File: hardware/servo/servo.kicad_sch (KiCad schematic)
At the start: 87 parts, among them J1 Midi In, J2 Midi Thru, J3 NeoPixel, J4 Power, J6 I2C0, J7 I2C1, M1 Motor_Servo, M10 Motor_Servo, M11 Motor_Servo, M12 Motor_Servo, M13 Motor_Servo, M14 Motor_Servo, M15 Motor_Servo, M16 Motor_Servo, M2 Motor_Servo, M3 Motor_Servo, M4 Motor_Servo, M5 Motor_Servo, M6 Motor_Servo, M7 Motor_Servo, M8 Motor_Servo, M9 Motor_Servo, Q1 BSS138, Q2 BSS138, Q3 TSM680P06, SW1 Reset, U1 6N138, U2 74AHC1G125, U3 74AHC1G125, U4 Raspberry Pi Pico, U5 AZ1117-5.0, U6 AZ1117-5.0, U7 GS8331

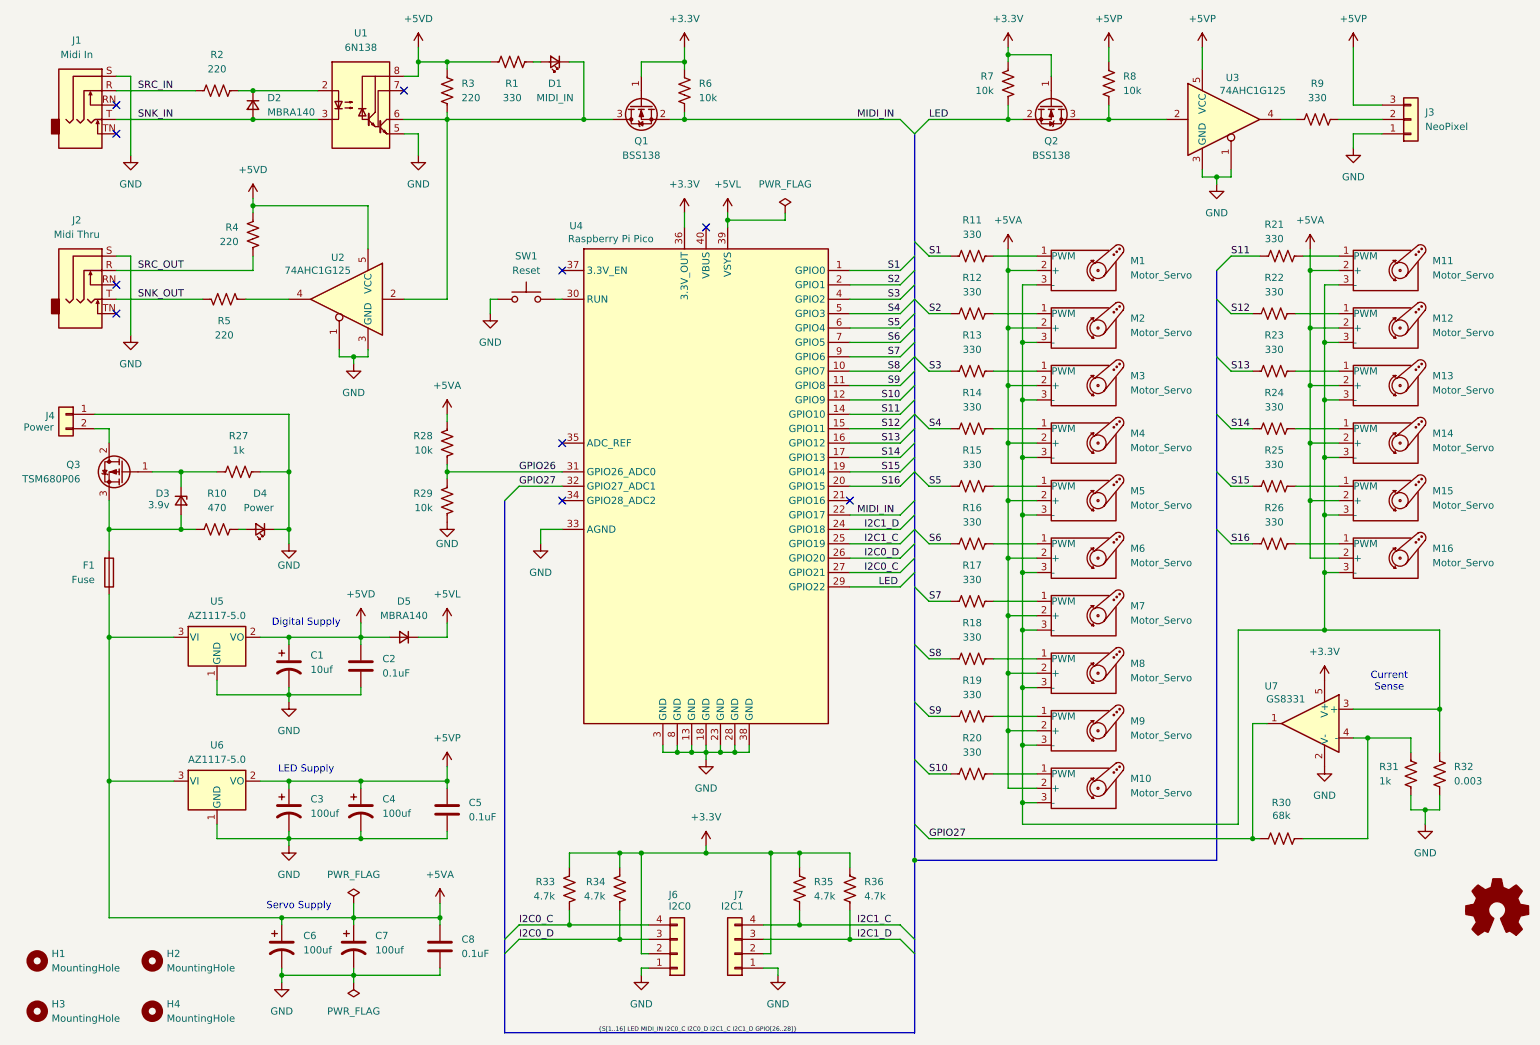
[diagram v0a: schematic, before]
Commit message: Rev 1.1: - Update to latest KiCad - Fixed short in servo board - Updates to right-angle diag connector on servo boards - Fixed microproc footprint on diag board - Flipped I2C connector to top of diag board - Pass all ERC and DRC checks, add exclusions
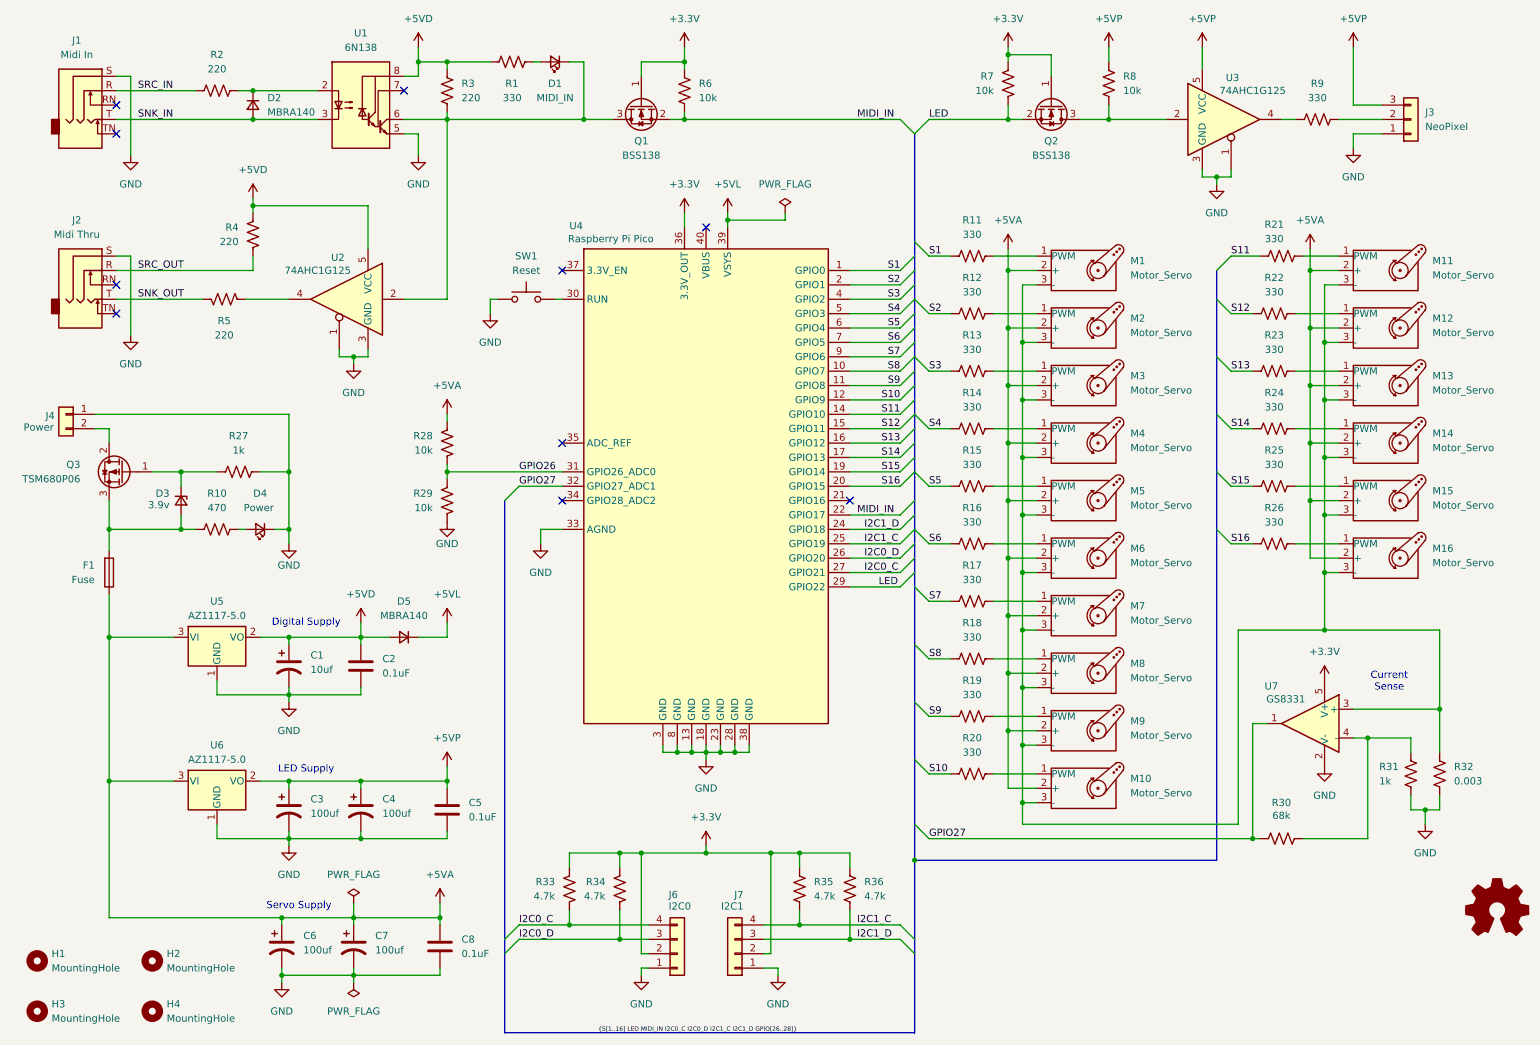
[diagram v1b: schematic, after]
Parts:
- J7: footprint Connector_JST:JST_SH_BM04B-SRSS-TB_1x04-1MP_P1.00mm_Vertical -> Connector_JST:JST_SH_SM04B-SRSS-TB_1x04-1MP_P1.00mm_Horizontal
- Q3: symbol Device:Q_PMOS_GDS -> Transistor_FET:Q_PMOS_GDS
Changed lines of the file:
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@@
 (kicad_sch
-	(version 20231120)
+	(version 20250114)
 	(generator "eeschema")
-	(generator_version "8.0")
+	(generator_version "9.0")
 	(paper "A4")
 	(title_block
 		(title "Animatronics - Servo (ANI-SRV)")
-		(date "2025-02-09")
-		(rev "1.0")
+		(date "2025-09-03")
+		(rev "1.1")
 		(company "Sparky Bobo Designs")
 		(comment 2 "Designed by: SparkyBobo")
@@
 		(comment 4 "Released under the Creative Commons Attribution Share-Alike 4.0 License")
 	)
+	(text "Current\nSense"
+		(exclude_from_sim no)
+		(at 257.81 133.604 0)
+		(effects
+			(font
+				(size 1.27 1.27)
+			)
+		)
+	)
+	(text "LED Supply"
+		(exclude_from_sim no)
+		(at 66.548 149.098 0)
+		(effects
+			(font
+				(size 1.27 1.27)
+			)
+		)
+	)
+	(text "Digital Supply"
+		(exclude_from_sim no)
+		(at 66.548 123.19 0)
+		(effects
+			(font
+				(size 1.27 1.27)
+			)
+		)
+	)
+	(text "Servo Supply"
+		(exclude_from_sim no)
+		(at 65.278 173.228 0)
+		(effects
+			(font
+				(size 1.27 1.27)
+			)
+		)
+	)
 	(junction
 		(at 246.38 114.3)
@@
 		)
 	)
-	(text "Current\nSense"
-		(exclude_from_sim no)
-		(at 257.81 133.604 0)
-		(effects
-			(font
-				(size 1.27 1.27)
-			)
-		)
-	)
-	(text "LED Supply"
-		(exclude_from_sim no)
-		(at 66.548 149.098 0)
-		(effects
-			(font
-				(size 1.27 1.27)
-			)
-		)
-	)
-	(text "Digital Supply"
-		(exclude_from_sim no)
-		(at 66.548 123.19 0)
-		(effects
-			(font
-				(size 1.27 1.27)
-			)
-		)
-	)
-	(text "Servo Supply"
-		(exclude_from_sim no)
-		(at 65.278 173.228 0)
-		(effects
-			(font
-				(size 1.27 1.27)
-			)
-		)
-	)
 	(label "S6"
 		(at 176.53 109.22 0)
@@
 			)
 		)
+		(property "Sim.Pin" "1=K 2=A"
+			(at 110.49 24.13 0)
+			(effects
+				(font
+					(size 1.27 1.27)
+				)
+				(hide yes)
+			)
+		)
 		(pin "2"
 		)
@@
 			)
 		)
+		(property "Sim.Enable" "0"
+			(at 276.86 173.99 0)
+			(effects
+				(font
+					(size 1.27 1.27)
+				)
+				(hide yes)
+			)
+		)
 		(instances
 			(project ""
@@
 			)
 		)
+		(property "Sim.Pin" "1=K 2=A"
+			(at 58.42 106.68 0)
+			(effects
+				(font
+					(size 1.27 1.27)
+				)
+				(hide yes)
+			)
+		)
 		(pin "2"
 		)
@@
 	)
 	(symbol
-		(lib_id "Device:Q_PMOS_GDS")
+		(lib_id "Transistor_FET:Q_PMOS_GDS")
 		(at 34.29 96.52 0)
 		(mirror y)
@@
 			)
 		)
-		(property "Footprint" "Connector_JST:JST_SH_BM04B-SRSS-TB_1x04-1MP_P1.00mm_Vertical"
+		(property "Footprint" "Connector_JST:JST_SH_SM04B-SRSS-TB_1x04-1MP_P1.00mm_Horizontal"
 			(at 142.24 181.61 0)
 			(effects
@@
 		)
 	)
+	(embedded_fonts no)
 )
